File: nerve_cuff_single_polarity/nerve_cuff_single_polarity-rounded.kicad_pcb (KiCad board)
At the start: 2 copper layers, 5 x 5.2 mm, 2 parts

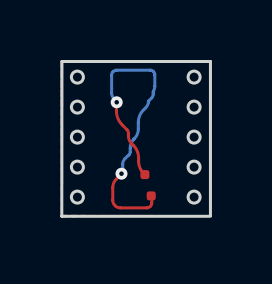
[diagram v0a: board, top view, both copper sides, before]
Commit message: adding rounded corners
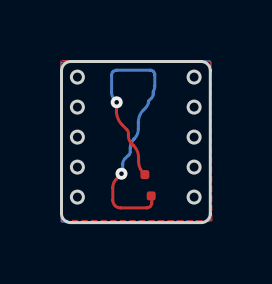
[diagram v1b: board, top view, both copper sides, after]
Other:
- board size 5 x 5.2 mm -> 5 x 5.4 mm
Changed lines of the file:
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@@
   (gr_circle (center 91.43 29) (end 91.63 29)
     (stroke (width 0.1) (type default)) (fill none) (layer "Edge.Cuts"))
+  (gr_arc (start 95.86 30.55) (mid 95.772132 30.762132) (end 95.56 30.85)
+    (stroke (width 0.1) (type default)) (layer "Edge.Cuts"))
   (gr_circle (center 91.43 28) (end 91.63 28)
     (stroke (width 0.1) (type default)) (fill none) (layer "Edge.Cuts"))
-  (gr_line (start 90.915 25.48) (end 90.91 30.635)
+  (gr_line (start 90.9 25.79) (end 90.9 30.55)
     (stroke (width 0.1) (type default)) (layer "Edge.Cuts"))
   (gr_circle (center 95.32 26) (end 95.52 26)
@@
   (gr_circle (center 95.32 28) (end 95.52 28)
     (stroke (width 0.1) (type default)) (fill none) (layer "Edge.Cuts"))
+  (gr_arc (start 95.55 25.48) (mid 95.767132 25.565797) (end 95.86 25.78)
+    (stroke (width 0.1) (type default)) (layer "Edge.Cuts"))
   (gr_circle (center 91.43 26) (end 91.63 26)
     (stroke (width 0.1) (type default)) (fill none) (layer "Edge.Cuts"))
-  (gr_line (start 95.865 30.61) (end 95.865 25.48)
+  (gr_line (start 95.86 30.55) (end 95.86 25.78)
     (stroke (width 0.1) (type default)) (layer "Edge.Cuts"))
   (gr_circle (center 95.32 30) (end 95.52 30)
     (stroke (width 0.1) (type default)) (fill none) (layer "Edge.Cuts"))
-  (gr_line (start 90.915 25.48) (end 95.865 25.48)
+  (gr_line (start 91.21 25.48) (end 95.55 25.48)
+    (stroke (width 0.1) (type default)) (layer "Edge.Cuts"))
+  (gr_arc (start 90.9 25.79) (mid 90.990797 25.570797) (end 91.21 25.48)
     (stroke (width 0.1) (type default)) (layer "Edge.Cuts"))
   (gr_circle (center 95.32 27) (end 95.52 27)
     (stroke (width 0.1) (type default)) (fill none) (layer "Edge.Cuts"))
-  (gr_line (start 90.91 30.64) (end 95.86 30.64)
+  (gr_arc (start 91.2 30.85) (mid 90.987868 30.762132) (end 90.9 30.55)
+    (stroke (width 0.1) (type default)) (layer "Edge.Cuts"))
+  (gr_line (start 95.56 30.85) (end 91.2 30.85)
     (stroke (width 0.1) (type default)) (layer "Edge.Cuts"))
   (gr_circle (center 91.43 30) (end 91.63 30)
@@
         (xy 95.27 25.48)
         (xy 90.88 25.45)
-        (xy 90.9 30.61)
-        (xy 95.88 30.62)
+        (xy 90.93 30.78)
+        (xy 95.91 30.79)
         (xy 95.88 25.49)
       )
@@
       (pts
         (xy 90.88 25.52)
-        (xy 90.9 30.66)
-        (xy 95.87 30.62)
+        (xy 90.89 30.83)
+        (xy 95.86 30.79)
         (xy 95.87 25.46)
         (xy 91.35 25.45)
